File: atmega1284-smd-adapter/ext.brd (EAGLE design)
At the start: 24.9 x 24.9 mm, 2 parts

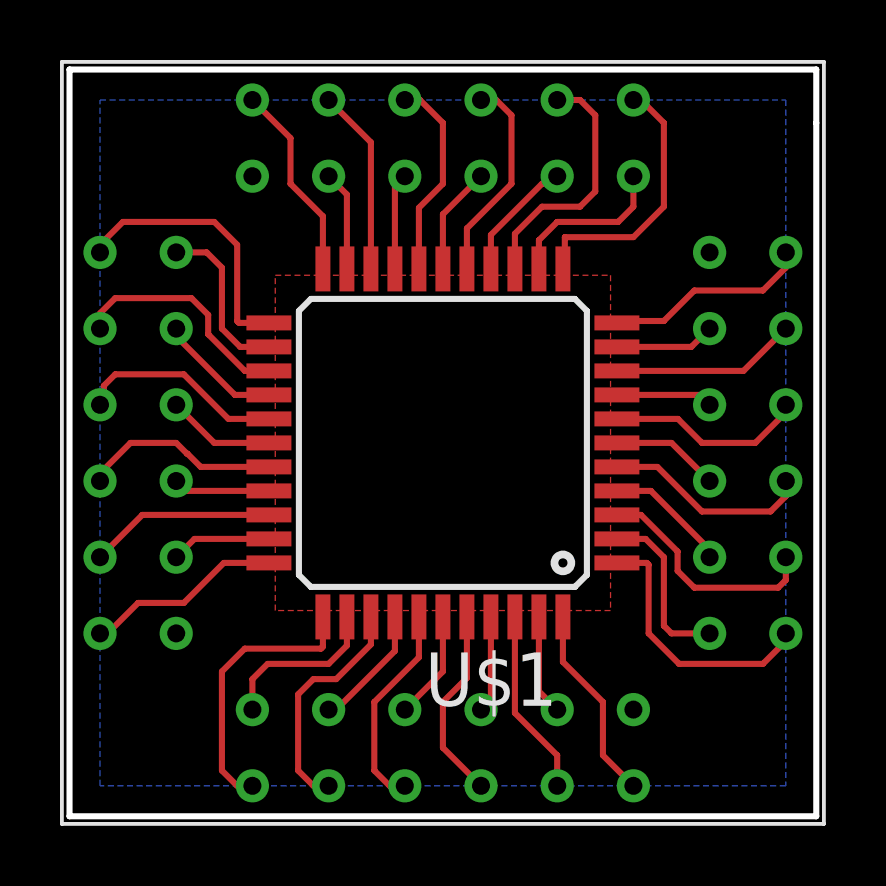
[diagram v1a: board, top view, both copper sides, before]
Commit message: [fix atmega1284p adapter drill size]
	- extend the drill size of the atmega1284p adapter
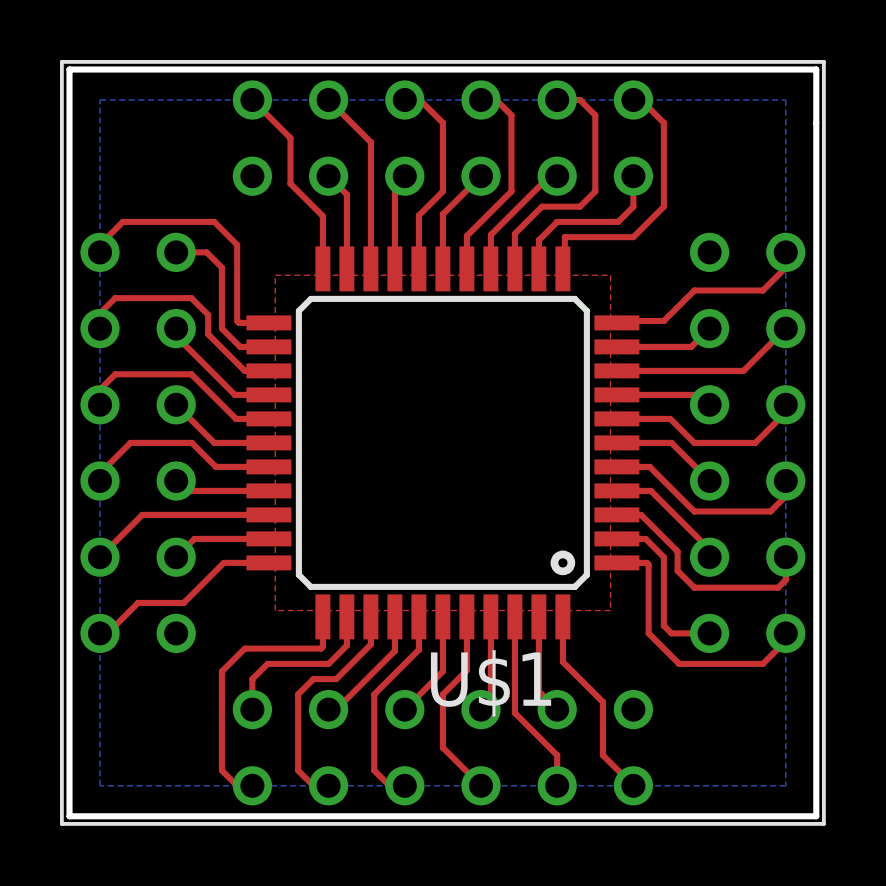
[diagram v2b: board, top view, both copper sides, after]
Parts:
- U$3: device 1284p.rpt:TQFP44-ADAPTER -> mega1284p:TQFP44-ADAPTER
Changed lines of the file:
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@@
 <attribute name="VALUE" x="43.76085" y="20.6750375" size="1.778" layer="27" rot="R180"/>
 </element>
-<element name="U$3" library="1284p.rpt" package="TQFP44-ADAPTER" value="MEGA1284P_ADAPTER" x="45.974" y="14.986" smashed="yes" rot="R180"/>
+<element name="U$3" library="mega1284p" package="TQFP44-ADAPTER" value="MEGA1284P_ADAPTER" x="45.974" y="14.986" smashed="yes" rot="R180"/>
 </elements>
 <signals>
@@
 <contactref element="U$1" pad="7"/>
 <contactref element="U$3" pad="P$7"/>
-<wire x1="46.694" y1="19.596" x2="48.73" y2="19.596" width="0.2032" layer="1"/>
-<wire x1="48.73" y1="19.596" x2="49.53" y2="18.796" width="0.2032" layer="1"/>
+<wire x1="46.694" y1="19.596" x2="48.476" y2="19.596" width="0.2032" layer="1"/>
+<wire x1="48.476" y1="19.596" x2="49.276" y2="18.796" width="0.2032" layer="1"/>
 <wire x1="52.324" y1="20.066" x2="52.324" y2="19.812" width="0.2032" layer="1"/>
 <wire x1="52.324" y1="19.812" x2="51.308" y2="18.796" width="0.2032" layer="1"/>
-<wire x1="49.53" y1="18.796" x2="51.308" y2="18.796" width="0.2032" layer="1"/>
+<wire x1="49.276" y1="18.796" x2="51.308" y2="18.796" width="0.2032" layer="1"/>
 </signal>
 <signal name="GND">
@@
 <wire x1="48.514" y1="18.796" x2="49.784" y2="17.526" width="0.2032" layer="1"/>
 <wire x1="33.274" y1="18.796" x2="32.004" y2="20.066" width="0.2032" layer="1"/>
-<wire x1="40.094" y1="26.632" x2="40.894" y2="27.432" width="0.2032" layer="1"/>
-<wire x1="40.894" y1="27.432" x2="40.894" y2="29.464" width="0.2032" layer="1"/>
+<wire x1="40.094" y1="26.378" x2="40.894" y2="27.178" width="0.2032" layer="1"/>
+<wire x1="40.894" y1="27.178" x2="40.894" y2="29.464" width="0.2032" layer="1"/>
 <wire x1="40.894" y1="29.464" x2="40.132" y2="30.226" width="0.2032" layer="1"/>
 <wire x1="40.132" y1="30.226" x2="39.624" y2="30.226" width="0.2032" layer="1"/>
@@
 <wire x1="40.894" y1="12.996" x2="40.894" y2="11.176" width="0.2032" layer="1"/>
 <wire x1="46.694" y1="18.796" x2="48.514" y2="18.796" width="0.2032" layer="1"/>
-<wire x1="40.094" y1="24.596" x2="40.094" y2="26.632" width="0.2032" layer="1"/>
+<wire x1="40.094" y1="24.596" x2="40.094" y2="26.378" width="0.2032" layer="1"/>
 <polygon width="0.2032" layer="16">
 <vertex x="29.464" y="7.366"/>
@@
 <wire x1="42.164" y1="27.686" x2="40.894" y2="26.416" width="0.2032" layer="1"/>
 <wire x1="40.894" y1="26.416" x2="40.894" y2="24.596" width="0.2032" layer="1"/>
-<wire x1="35.094" y1="17.996" x2="32.82036875" y2="17.996" width="0.2032" layer="1"/>
-<wire x1="32.82036875" y1="17.996" x2="32.38076875" y2="18.4356" width="0.2032" layer="1"/>
-<wire x1="32.38076875" y1="18.4356" x2="32.3644" y2="18.4356" width="0.2032" layer="1"/>
-<wire x1="32.3644" y1="18.4356" x2="32.004" y2="18.796" width="0.2032" layer="1"/>
-<wire x1="32.004" y1="18.796" x2="30.48" y2="18.796" width="0.2032" layer="1"/>
+<wire x1="35.094" y1="17.996" x2="33.32836875" y2="17.996" width="0.2032" layer="1"/>
+<wire x1="33.32836875" y1="17.996" x2="32.52836875" y2="18.796" width="0.2032" layer="1"/>
+<wire x1="32.52836875" y1="18.796" x2="30.48" y2="18.796" width="0.2032" layer="1"/>
 <wire x1="30.48" y1="18.796" x2="29.464" y2="17.78" width="0.2032" layer="1"/>
 <wire x1="29.464" y1="17.78" x2="29.464" y2="17.526" width="0.2032" layer="1"/>
-<wire x1="29.464" y1="20.066" x2="29.591" y2="19.939" width="0.2032" layer="1"/>
-<wire x1="40.094" y1="12.996" x2="40.094" y2="11.646" width="0.2032" layer="1"/>
-<wire x1="40.094" y1="11.646" x2="38.608" y2="10.16" width="0.2032" layer="1"/>
-<wire x1="38.608" y1="10.16" x2="38.608" y2="7.874" width="0.2032" layer="1"/>
+<wire x1="40.094" y1="12.996" x2="40.094" y2="11.9" width="0.2032" layer="1"/>
+<wire x1="40.094" y1="11.9" x2="38.608" y2="10.414" width="0.2032" layer="1"/>
+<wire x1="38.608" y1="10.414" x2="38.608" y2="7.874" width="0.2032" layer="1"/>
 <wire x1="39.116" y1="7.366" x2="39.624" y2="7.366" width="0.2032" layer="1"/>
 <wire x1="38.608" y1="7.874" x2="39.116" y2="7.366" width="0.2032" layer="1"/>
-<wire x1="46.694" y1="17.996" x2="48.044" y2="17.996" width="0.2032" layer="1"/>
-<wire x1="48.044" y1="17.996" x2="49.53" y2="16.51" width="0.2032" layer="1"/>
-<wire x1="49.53" y1="16.51" x2="51.816" y2="16.51" width="0.2032" layer="1"/>
+<wire x1="46.694" y1="17.996" x2="47.79" y2="17.996" width="0.2032" layer="1"/>
+<wire x1="47.79" y1="17.996" x2="49.276" y2="16.51" width="0.2032" layer="1"/>
+<wire x1="49.276" y1="16.51" x2="51.816" y2="16.51" width="0.2032" layer="1"/>
 <wire x1="51.816" y1="16.51" x2="52.324" y2="17.018" width="0.2032" layer="1"/>
 <wire x1="52.324" y1="17.018" x2="52.324" y2="17.526" width="0.2032" layer="1"/>
-<wire x1="35.094" y1="19.596" x2="33.744" y2="19.596" width="0.2032" layer="1"/>
-<wire x1="33.744" y1="19.596" x2="32.258" y2="21.082" width="0.2032" layer="1"/>
-<wire x1="32.258" y1="21.082" x2="29.972" y2="21.082" width="0.2032" layer="1"/>
-<wire x1="29.591" y1="20.701" x2="29.591" y2="19.939" width="0.2032" layer="1"/>
-<wire x1="29.972" y1="21.082" x2="29.591" y2="20.701" width="0.2032" layer="1"/>
+<wire x1="35.094" y1="19.596" x2="33.998" y2="19.596" width="0.2032" layer="1"/>
+<wire x1="33.998" y1="19.596" x2="32.512" y2="21.082" width="0.2032" layer="1"/>
+<wire x1="29.972" y1="21.082" x2="32.512" y2="21.082" width="0.2032" layer="1"/>
 <polygon width="0.2032" layer="1">
 <vertex x="35.306" y="24.384"/>
@@
 <vertex x="35.306" y="13.208"/>
 </polygon>
+<wire x1="29.464" y1="20.066" x2="29.464" y2="20.574" width="0.2032" layer="1"/>
+<wire x1="29.464" y1="20.574" x2="29.972" y2="21.082" width="0.2032" layer="1"/>
 </signal>
 <signal name="MOSI">
@@
 <contactref element="U$3" pad="P$17"/>
 <contactref element="U$1" pad="16"/>
-<wire x1="41.694" y1="24.596" x2="41.694" y2="25.946" width="0.2032" layer="1"/>
-<wire x1="41.694" y1="25.946" x2="43.18" y2="27.432" width="0.2032" layer="1"/>
-<wire x1="43.18" y1="27.432" x2="43.18" y2="29.718" width="0.2032" layer="1"/>
+<wire x1="41.694" y1="24.596" x2="41.694" y2="25.692" width="0.2032" layer="1"/>
+<wire x1="41.694" y1="25.692" x2="43.18" y2="27.178" width="0.2032" layer="1"/>
+<wire x1="43.18" y1="27.178" x2="43.18" y2="29.718" width="0.2032" layer="1"/>
 <wire x1="42.672" y1="30.226" x2="42.164" y2="30.226" width="0.2032" layer="1"/>
 <wire x1="43.18" y1="29.718" x2="42.672" y2="30.226" width="0.2032" layer="1"/>
@@
 <contactref element="U$1" pad="40"/>
 <contactref element="U$3" pad="P$43"/>
-<wire x1="41.694" y1="10.96" x2="40.894" y2="10.16" width="0.2032" layer="1"/>
+<wire x1="41.694" y1="11.214" x2="40.894" y2="10.414" width="0.2032" layer="1"/>
 <wire x1="40.894" y1="8.636" x2="42.164" y2="7.366" width="0.2032" layer="1"/>
-<wire x1="40.894" y1="10.16" x2="40.894" y2="8.636" width="0.2032" layer="1"/>
-<wire x1="41.694" y1="12.996" x2="41.694" y2="10.96" width="0.2032" layer="1"/>
+<wire x1="40.894" y1="10.414" x2="40.894" y2="8.636" width="0.2032" layer="1"/>
+<wire x1="41.694" y1="12.996" x2="41.694" y2="11.214" width="0.2032" layer="1"/>
 </signal>
 <signal name="CLK0">
